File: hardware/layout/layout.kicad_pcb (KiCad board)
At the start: 4 copper layers, 50 x 22 mm, 74 parts, among them J1 208658-1001, J2 USB4105-GF-A-060, Q1 2N7002, SW1 TS-1088-AR02016, U1 PCA9306DCTR, U2 AP2112K-3.3TRG1, U3 USBLC6-2SC6, U4 W25Q16JVSSIQ, U5 RP2040, Y1 X322512MSB4SI

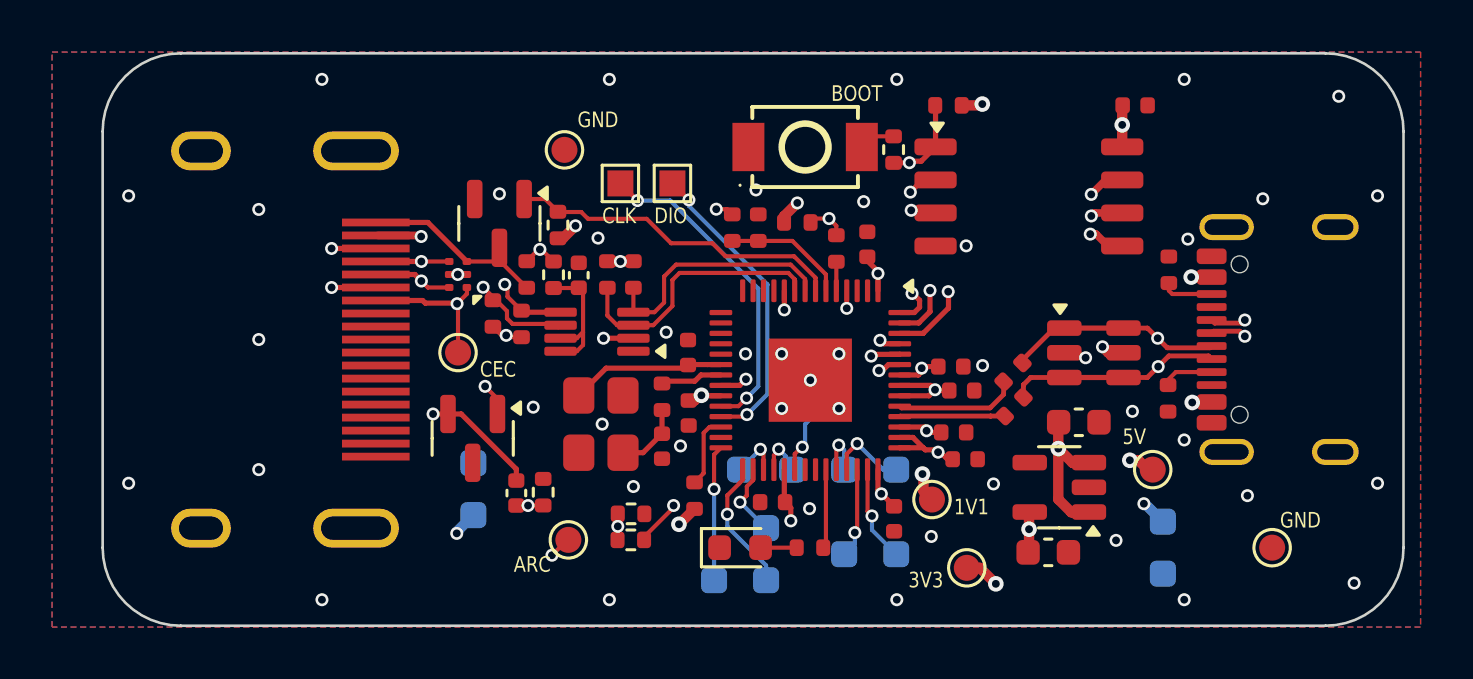
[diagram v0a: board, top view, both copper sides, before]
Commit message: hardware: QSPI reroute, board shrink, things moved here and there
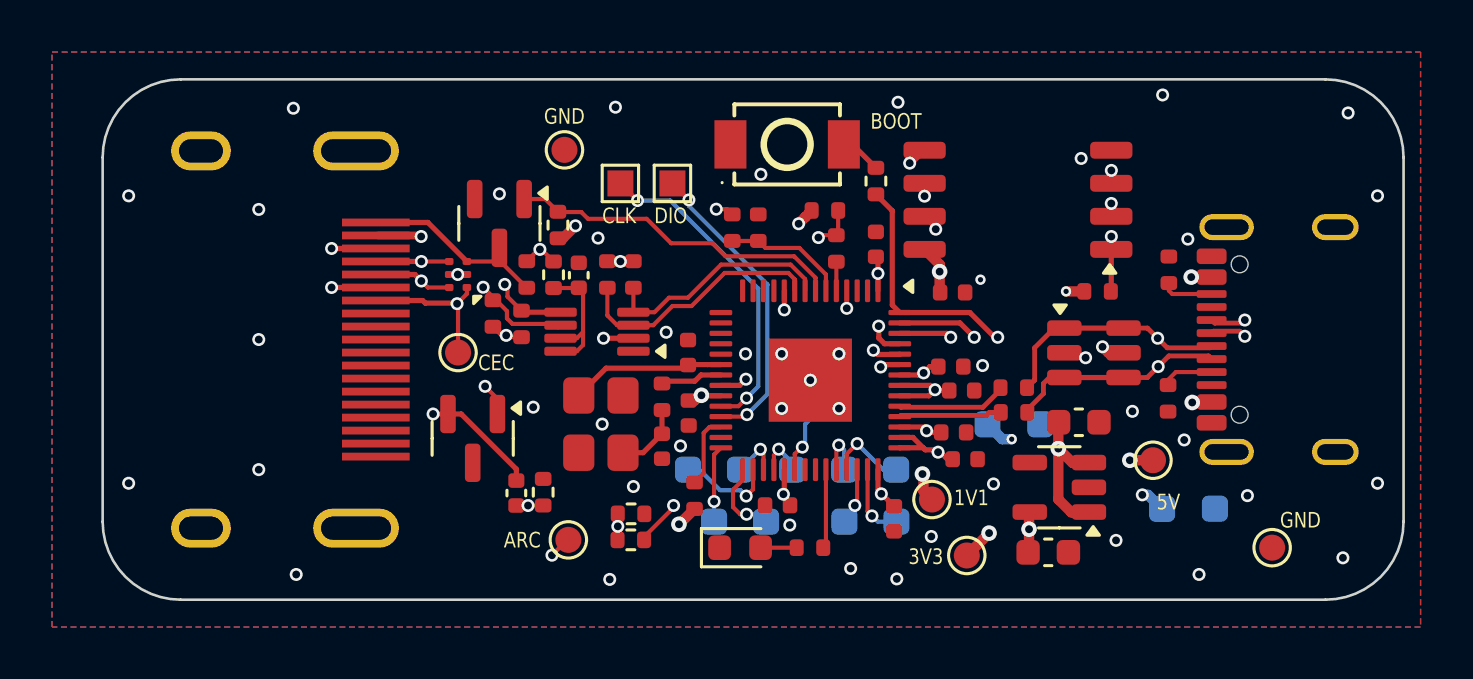
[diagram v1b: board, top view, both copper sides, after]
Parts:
- moved TP3 21.8 mm to (136.0, 114.3)
- moved TP1 20.1 mm to (134.0, 114.3)
- moved C5 10.0 mm to (132.7, 109.2)
- moved R19 9.16 mm to (138.2, 109.2), turned to 180 degrees
- moved TP7 3.75 mm to (122.5, 116.0)
- moved TP4 3.20 mm to (142.8, 117.5)
- moved TP5 2.25 mm to (123.5, 118.0)
- moved TP6 2.25 mm to (125.5, 118.0)
- moved R16 1.39 mm to (129.7, 104.9)
- moved TP13 1.25 mm to (128.5, 118.0)
- moved TP14 1.25 mm to (130.5, 118.0)
- moved R1 1.16 mm to (127.8, 106.0)
- moved SW1 0.70 mm to (126.3, 103.5)
- moved R22 0.59 mm to (135.0, 112.8), turned to 0 degrees
- moved TP2 0.49 mm to (140.7, 117.5)
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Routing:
- net QSPI_IO3: track 15.6 -> 7.61 mm
- net QSPI_CS: track 10.8 -> 17.4 mm
- net QSPI_CLK: track 13.7 -> 8.34 mm
- net QSPI_IO2: track 7.86 -> 11.7 mm
- net QSPI_IO0: track 12.2 -> 8.96 mm
- net QSPI_IO1: track 7.98 -> 11.1 mm
- net GP17: track 5.20 -> 2.95 mm
- net GP18: track 5.11 -> 3.10 mm
- net GP28: track 3.46 -> 2.20 mm
- net CEC_NODE: track 23.7 -> 22.5 mm
- net GP19: track 2.87 -> 3.80 mm
- net USB_D_P: track 13.2 -> 14.1 mm
- net GP29: track 3.71 -> 2.88 mm
- net VDD_3V3: track 24.8 -> 24.1 mm
- net DDC_SDA: track 9.56 -> 8.98 mm
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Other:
- board size 50 x 22 mm -> 50 x 20 mm

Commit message: hardware: add backside silkscreen
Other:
- board text added: "${PCB_GIT_HASH}"
- board text added: "@naorunaoru"
- board text added: "picoARC"
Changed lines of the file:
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@@
+		)
+	)
+	(gr_text "${PCB_GIT_HASH}"
+		(at 120.72 104.31 0)
+		(layer "B.SilkS")
+		(effects
+			(font
+				(size 0.6 0.5)
+				(thickness 0.1)
+			)
+			(justify left bottom mirror)
+		)
+	)
+	(gr_text "@naorunaoru"
+		(at 132.58 108.19 0)
+		(layer "B.SilkS")
+		(effects
+			(font
+				(size 1 1)
+				(thickness 0.1)
+			)
+			(justify left bottom mirror)
+		)
+	)
+	(gr_text "picoARC"
+		(at 132.9 106.28 0)
+		(layer "B.SilkS")
+		(effects
+			(font
+				(size 2 2)
+				(thickness 0.1)
+			)
+			(justify left bottom mirror)
 		)
 	)

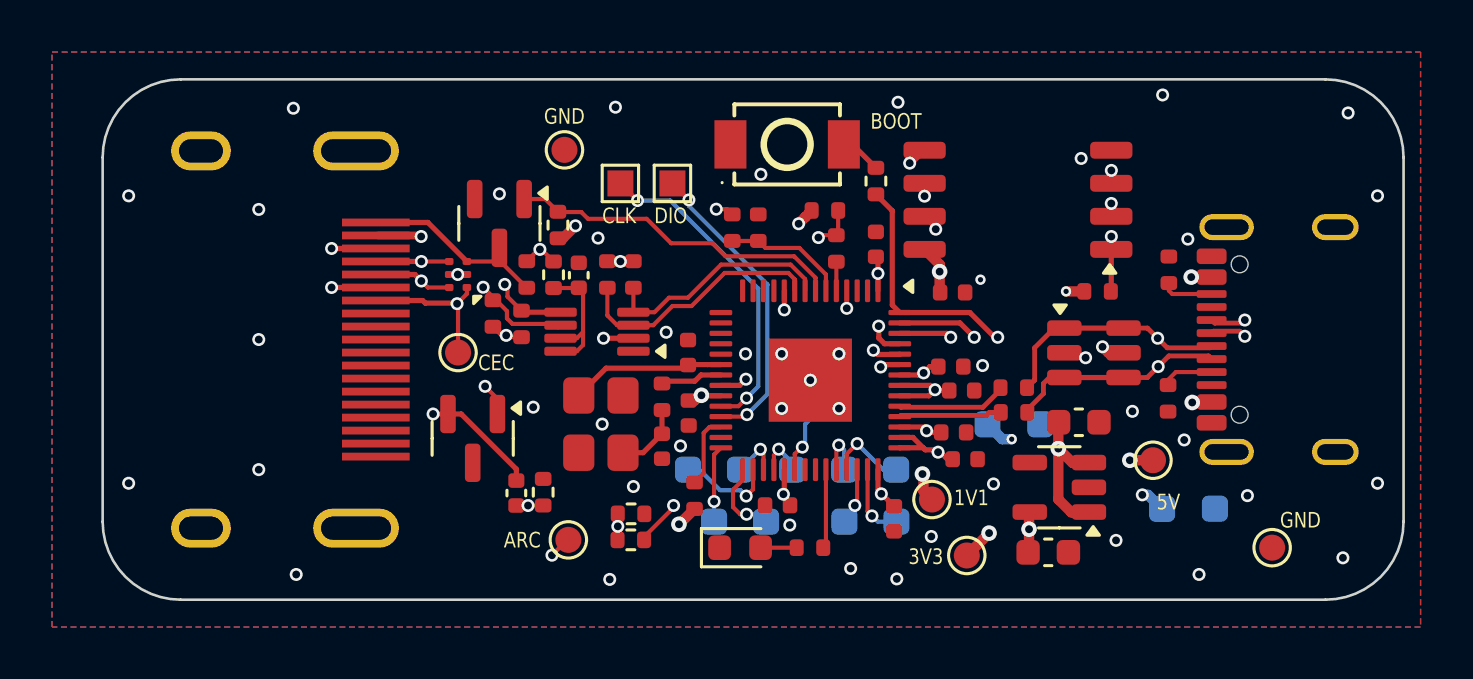
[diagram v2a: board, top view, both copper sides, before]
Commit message: hardware: consolidate HDMI ESD into 5-ch array + single +5V TVS
Replace the JLC-shortfall PESD5V0L4UF (4-ch, SOT-886, not LCSC-stocked) and
the PESD5V0S2BT (2-ch) with one 5-channel bidirectional array, D5V0M5B6LP16-7
(C445551), covering CEC/HPD/DDC_SDA_5V/DDC_SCL_5V/ARC, plus a single
bidirectional TVS H5VL10B (C7420372) on the cable +5V. Both LCSC-stocked.

- Add local footprints + symbols (array I/O pins renamed IO1/IO3/IO4/IO5/IO6
  since the LCSC-generated symbol names all five "I/O", unaddressable by the
  pins-by-name binding) and .wrl 3D models.
- Drop the D3 SOD-882 pin-1 silk circle that clipped pad-1 mask.
- Update jlcpcb-lcsc overlay; re-sync layout. DRC 0/0, make fab clean.
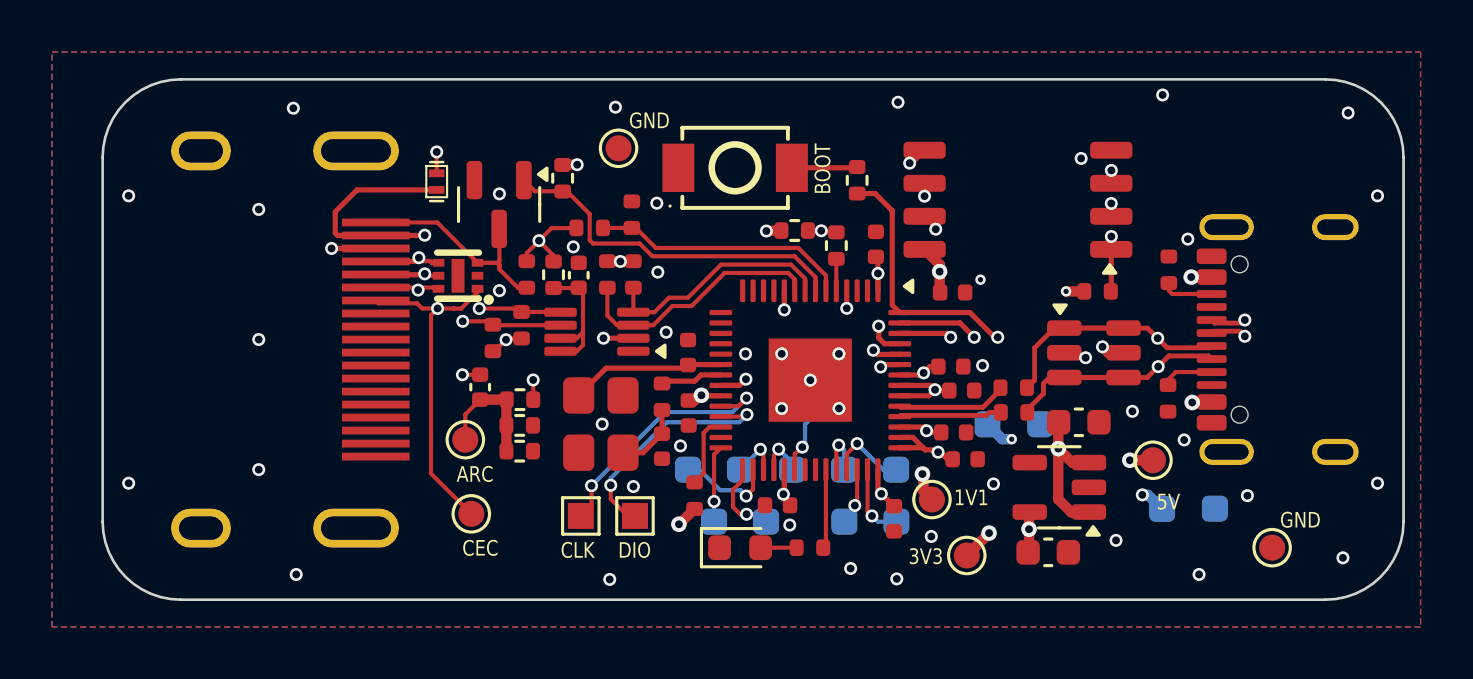
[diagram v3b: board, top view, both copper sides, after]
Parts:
- D2: value PESD5V0L4UF -> D5V0M5B6LP16-7; footprint kicad_libraries_kicad-footprints_Package_TO_SOT_SMD@9.0.3:SOT-886 -> naorunaoru_picoarc_footprints_picoarc:DFN1616-6_L1.6-W1.6-P0.50-BL-EP
- D3: value PESD5V0S2BT,215 -> H5VL10B; footprint kicad_libraries_kicad-footprints_Package_TO_SOT_SMD@9.0.3:SOT-23 -> naorunaoru_picoarc_footprints_picoarc:SOD-882_L1.0-W0.6-BI
- moved TP22 12.9 mm to (118.4, 117.8)
- moved TP23 12.9 mm to (120.5, 117.8)
- moved D3 9.97 mm to (112.8, 104.9), turned to 90 degrees
- moved R3 6.87 mm to (116.0, 113.3)
- moved TP19 6.22 mm to (114.2, 117.7)
- moved TP18 5.52 mm to (113.9, 114.8)
- moved R6 5.48 mm to (118.7, 106.7), turned to 0 degrees
- moved R14 4.91 mm to (116.0, 115.3)
- moved R7 4.89 mm to (120.3, 106.2)
- moved C1 4.30 mm to (114.5, 112.8)
- moved R15 2.72 mm to (116.0, 114.3), turned to 0 degrees
- moved SW1 2.19 mm to (124.3, 104.4)
- moved TP21 2.08 mm to (119.8, 103.7)
- moved R13 1.81 mm to (117.7, 104.8), turned to 90 degrees
- moved R1 1.39 mm to (126.6, 106.8)
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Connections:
- D2 pad 5: GND -> DDC_SCL_5V
- D2 pad 6: DDC_SCL_5V -> HDMI._ARC14
- D3 pad 2: HDMI._ARC14 -> GND
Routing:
- net CEC_NODE: track 22.5 -> 31.1 mm
- net HDMI._HDMI_5V: track 6.37 -> 13.5 mm, vias 5 -> 3
- net HDMI._ARC14: track 13.1 -> 7.08 mm
- net HDMI_5V_SENSE: track 4.76 -> 9.91 mm
- net SWD_SWCLK: track 12.5 -> 9.80 mm
- net SWD_SWDIO: track 11.8 -> 9.28 mm
- net ATT_A: track 2.88 -> 4.78 mm, vias 3 -> 0
- net ARC_TX: track 13.0 -> 14.6 mm
- net HDMI._HPD: track 7.38 -> 8.49 mm
- net BOOTSEL_SW: track 1.60 -> 2.52 mm
- net HPD_GATE: track 13.0 -> 13.9 mm
- net QSPI_CS: track 17.4 -> 18.1 mm
- net DDC_SCL_5V: track 9.36 -> 8.68 mm
- net GND: track 2.38 -> 2.52 mm, vias 46 -> 47
- removed copper zone on In1.Cu, net ATT_A

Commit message: hardware: replace HDMI 5V TVS
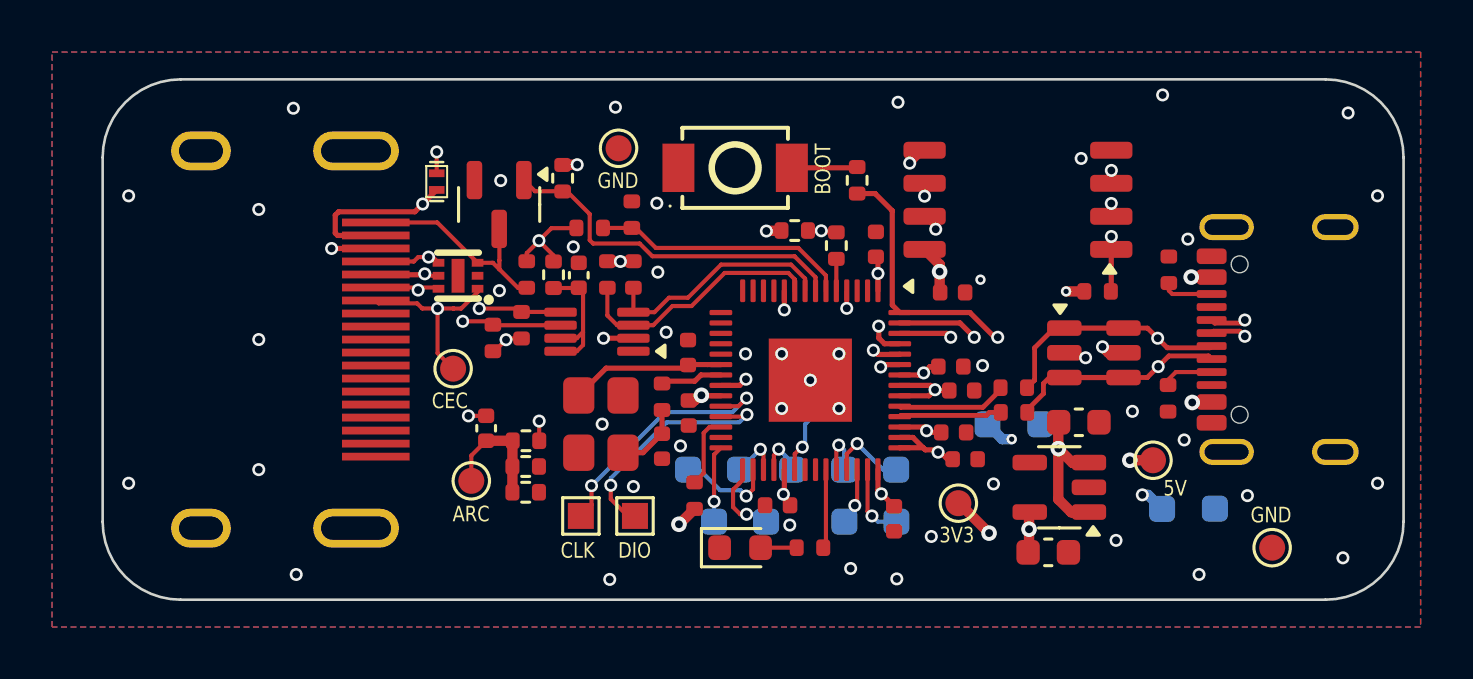
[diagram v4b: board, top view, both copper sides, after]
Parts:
- removed TP15: ?, kicad_libraries_kicad-footprints_TestPoint@9.0.3:TestPoint_Pad_D1.0mm
- D3: value H5VL10B -> H7VN10B
- moved TP19 5.62 mm to (113.5, 112.1)
- moved TP16 2.04 mm to (132.9, 117.3)
- moved TP18 1.60 mm to (114.2, 116.4)
- moved R14 1.60 mm to (116.3, 116.9)
- moved R15 1.60 mm to (116.3, 115.9)
- moved C1 1.60 mm to (114.7, 114.4)
- moved R3 1.60 mm to (116.3, 114.9)
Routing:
- net CEC_NODE: track 31.1 -> 25.0 mm
- net HDMI._HDMI_5V: track 13.5 -> 11.6 mm
- net HDMI._ARC14: track 7.08 -> 8.75 mm
- net VDD_1V1: track 5.84 -> 4.70 mm, vias 4 -> 3
- net ARC_TX: track 14.6 -> 15.7 mm
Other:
- board text removed: "1V1"

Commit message: hardware/layout: fix sub-spec vias, add orientation silk, D3 cathode
Resolve JLCPCB order 12939101A_Y2 + assembly-orientation cleanup:

  - 3 stitching vias were 0.2mm drill / 0.4mm pad (0.1mm annular), which JLC
    flagged for a mandatory paid 4-wire Kelvin test. Resized to the standard
    0.3mm/0.5mm stitching via and refilled all zones (the larger pad needs
    the GND/VDD planes to pull back, or DRC throws clearance errors).
  - Added F.SilkS orientation indicators to the polarized 2-pin parts whose
    marks the earlier silk-strip pass had removed: D1 LED cathode bar,
    Y1 crystal pin-1 dot, D3 TVS cathode bar (placed outside the courtyards;
    DRC stays clean). ICs/Q1 (POLY pin-1) and D2 (CIRCLE dots) already marked.
  - D3: refreshed embedded value to H7VH10U + cathode bar (see TVS swap).

DRC: 0 violations.
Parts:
- D3: value H7VN10B -> H7VH10U
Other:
- board text added: "JLCJLCJLCJLC"
